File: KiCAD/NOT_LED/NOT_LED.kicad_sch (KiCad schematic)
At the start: 8 parts, among them J1 Conn_01x02_Pin, J3 Conn_01x02_Pin, Q13 2N7000, Q3 2N7000, Y1 Conn_01x01_Pin

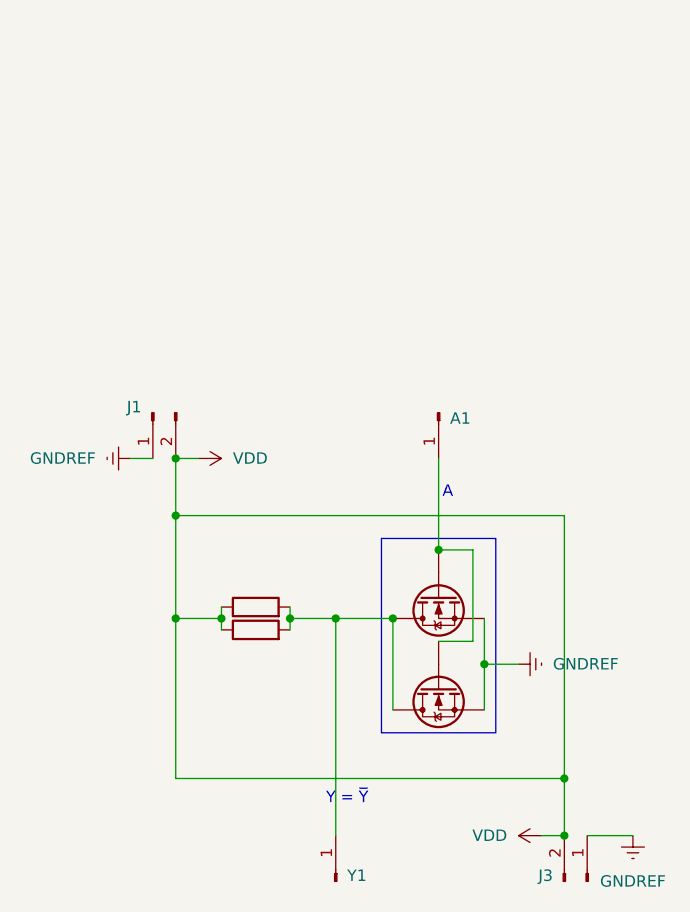
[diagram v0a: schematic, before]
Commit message: KiCAD: NOT_LED
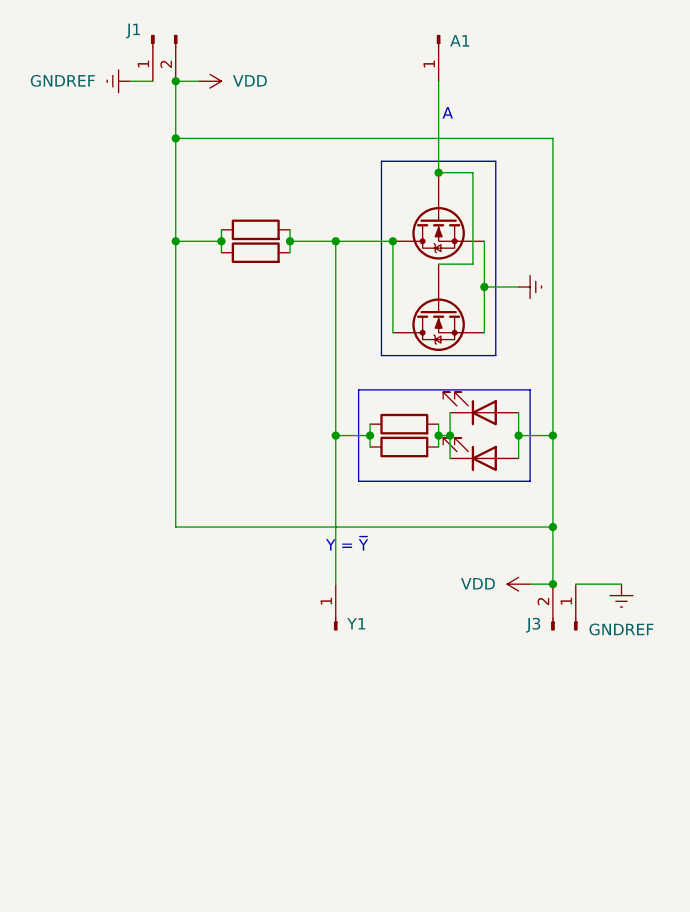
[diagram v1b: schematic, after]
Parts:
- added D1: LED, LED_THT:LED_D1.8mm_W3.3mm_H2.4mm, symbol Device:LED
- added D11: LED, LED_SMD:LED_1206_3216Metric, symbol Device:LED
- added R13: R, Resistor_SMD:R_1206_3216Metric, symbol Device:R
- added R3: R, Resistor_THT:R_Axial_DIN0207_L6.3mm_D2.5mm_P10.16mm_Horizontal, symbol Device:R
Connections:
- net VDD: now also D1.2 (A), D11.2 (A)
- net at Q13.3 (D), Q3.3 (D), R15.2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: now also R13.1, R3.1
- new net: D1.1 (K), D11.1 (K), R13.2, R3.2
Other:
- moved on the sheet: A1, J1, J3, Y1
